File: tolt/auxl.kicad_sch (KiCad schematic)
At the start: 2 parts, among them U17 BMI160, U18 ESP32-C3_SUPERMINI_SMD

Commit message: Reapply "Merge branch 'main' of https://github.com/LJBoxx/bigtolt"
This reverts commit 10d1035653869a11abcc4dc45a35a471baa73785.
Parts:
- added C78: 2.2u, Capacitor_SMD:C_0603_1608Metric, symbol Device:C
- added C79: 100n, Capacitor_SMD:C_0402_1005Metric, symbol Device:C
- added C83, C84: 4.7u, Capacitor_SMD:C_0805_2012Metric, symbol Device:C
- added R70, R71: 1k, Resistor_SMD:R_0603_1608Metric, symbol Device:R
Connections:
- net +5V: now also C83.2, C84.2
- net GND: now also U17.6 (GNDIO), U17.7 (GND), C78.1, C79.1, C83.1, C84.1
- net scl_bmi: now reaches U17.13 (SCx)
- net scl_bmi: now also R71.2
- net sda_bmi: now reaches U17.14 (SDx)
- net sda_bmi: now also R70.2
- net VCC: now reaches U17.5 (VDDIO)
- net VCC: now also U17.8 (VDD), C78.2, C79.2, R70.1, R71.1
- no-connect marks 12 -> 20
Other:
- moved on the sheet: U17, U18

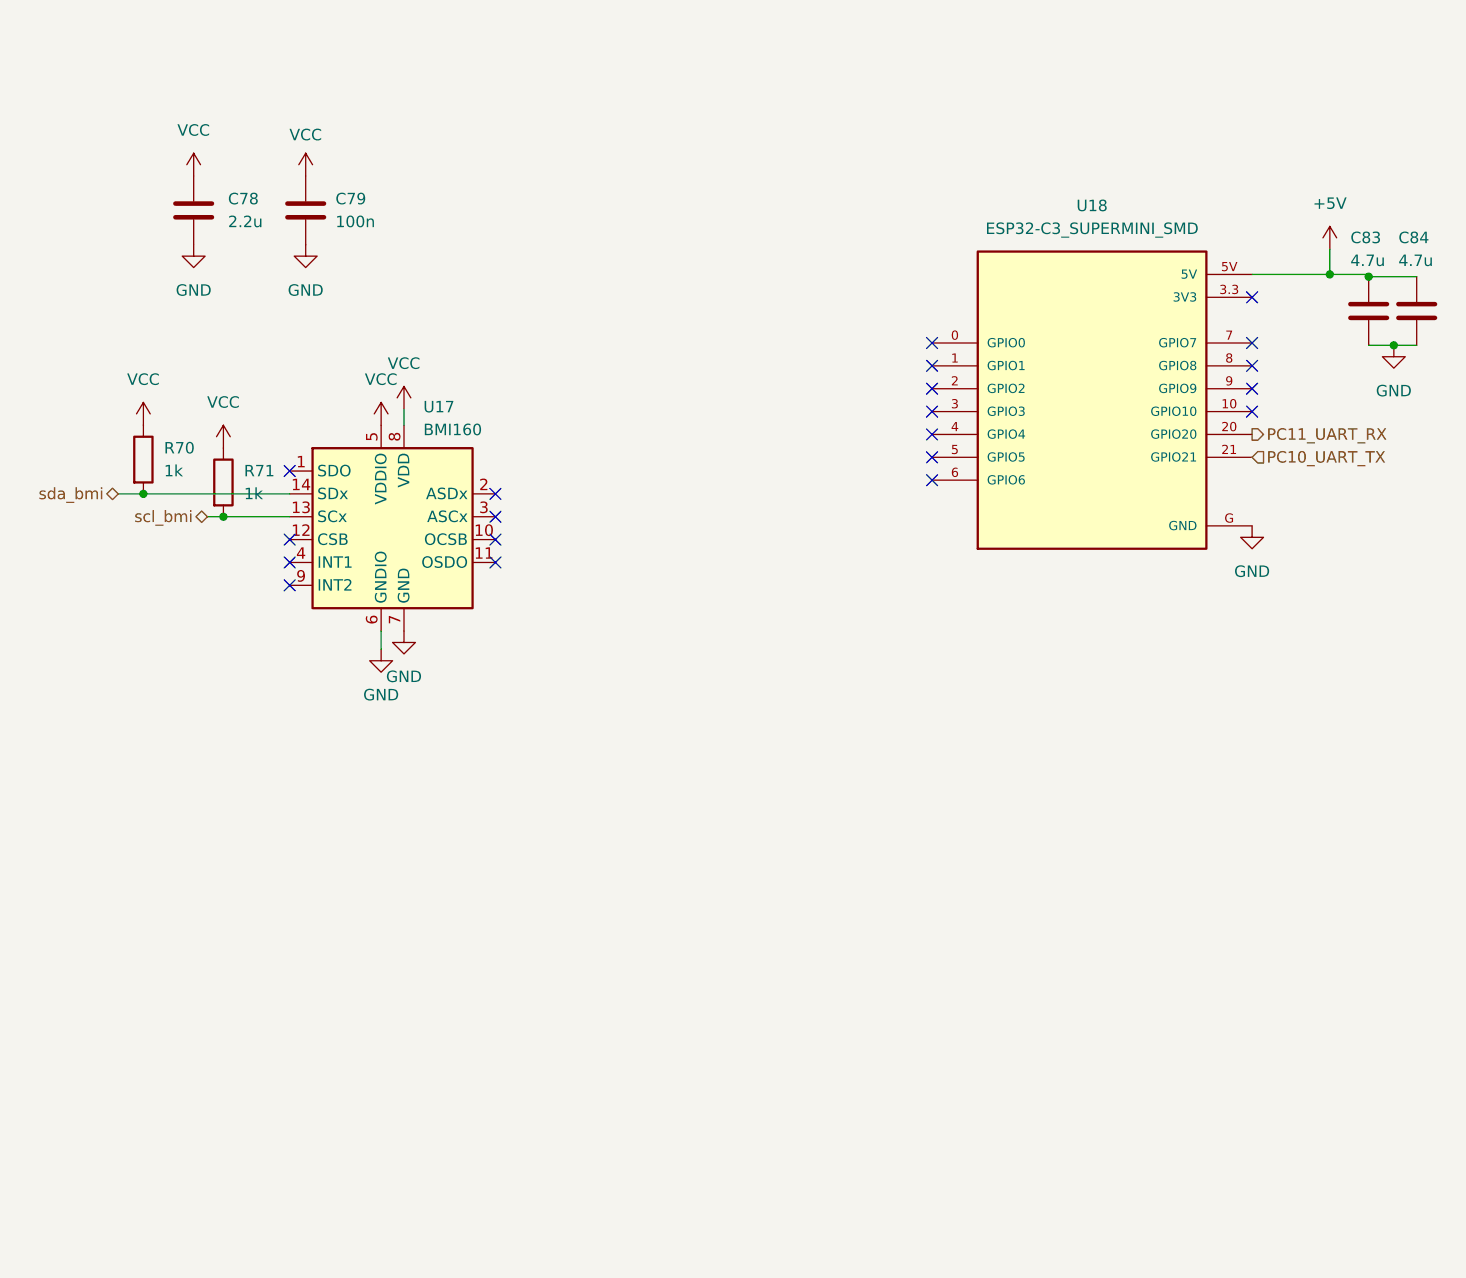
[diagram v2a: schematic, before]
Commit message: Revert "Merge branch 'main' of https://github.com/LJBoxx/bigtolt"
This reverts commit 648dc93627ac55c8b54fa74faadbb35a312ea564, reversing
changes made to 972c1c2491e13322900779e00755fdd65e6f8c8a.
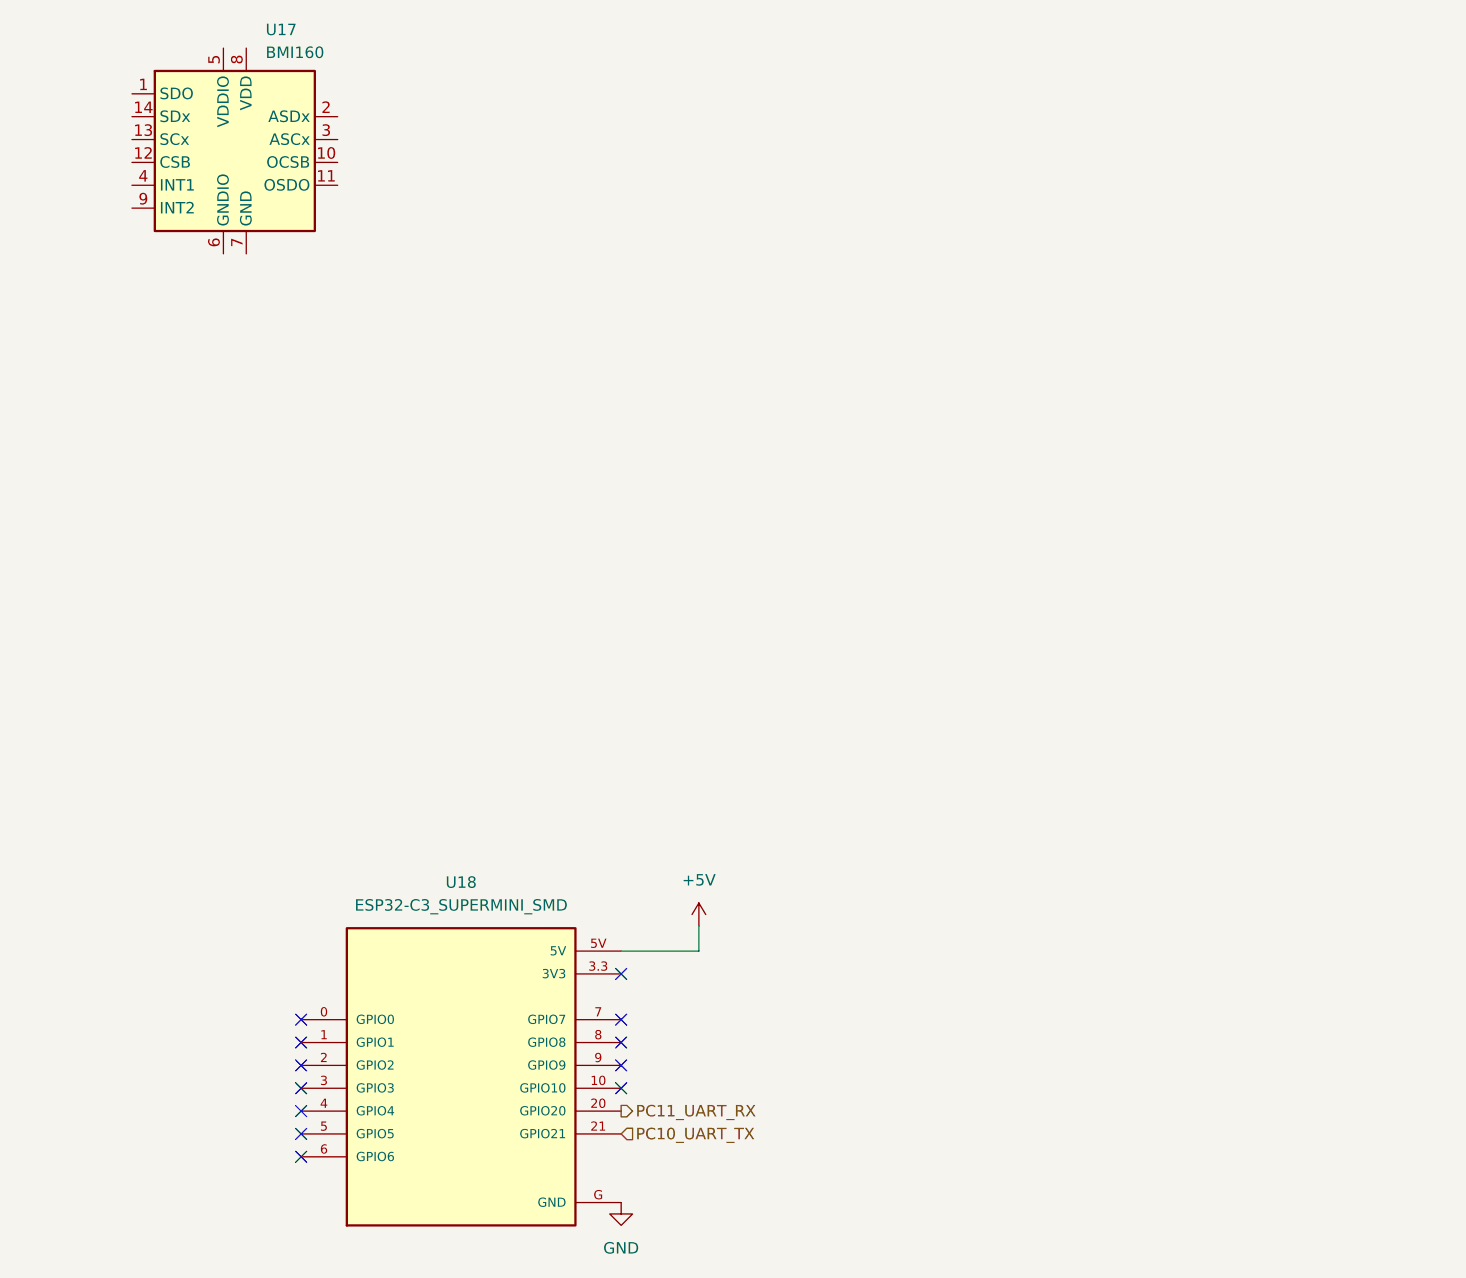
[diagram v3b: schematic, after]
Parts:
- removed C78: 2.2u, Capacitor_SMD:C_0603_1608Metric, symbol Device:C
- removed C79: 100n, Capacitor_SMD:C_0402_1005Metric, symbol Device:C
- removed C83, C84: 4.7u, Capacitor_SMD:C_0805_2012Metric, symbol Device:C
- removed R70, R71: 1k, Resistor_SMD:R_0603_1608Metric, symbol Device:R
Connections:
- net GND: no longer U17.6 (GNDIO), U17.7 (GND)
- net VCC: no longer names the net of U17.5 (VDDIO)
- net VCC: no longer U17.8 (VDD)
- net scl_bmi: no longer names the net of U17.13 (SCx)
- net sda_bmi: no longer names the net of U17.14 (SDx)
- no-connect marks 20 -> 12
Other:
- moved on the sheet: U17, U18
